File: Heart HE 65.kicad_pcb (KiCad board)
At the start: 2 copper layers, 303.8 x 94.2 mm, 290 parts, among them J2 Conn_01x04, SW1 SW_Push, U10 SLSS49E-3, U100 SLSS49E-3, U101 SLSS49E-3, U102 SLSS49E-3, U103 SLSS49E-3, U104 SLSS49E-3, U11 SLSS49E-3, U12 SLSS49E-3, U14 SLSS49E-3, U15 SLSS49E-3, U16 SLSS49E-3, U17 SLSS49E-3, U18 SLSS49E-3, U19 AP2112K-3.3, U2 74HC4051, U20 SLSS49E-3, U21 SLSS49E-3, U22 SLSS49E-3, U23 SLSS49E-3, U24 SLSS49E-3, U25 SLSS49E-3, U26 SLSS49E-3, U27 AT32F405KxU7-4, U28 SLSS49E-3, U29 SLSS49E-3, U3 SLSS49E-3, U30 SLSS49E-3, U31 SLSS49E-3, U32 74HC4051, U33 SLSS49E-3, U34 SLSS49E-3, U35 SLSS49E-3, U36 SLSS49E-3, U37 SLSS49E-3, U38 74HC4051, U4 SLSS49E-3, U40 SLSS49E-3, U41 SLSS49E-3, U42 SLSS49E-3, U43 SLSS49E-3, U44 SLSS49E-3, U45 74HC4051, U46 SLSS49E-3, U47 SLSS49E-3, U48 SLSS49E-3, U49 SLSS49E-3, U5 SLSS49E-3, U51 74HC4051, U52 SLSS49E-3, U53 SLSS49E-3, U54 SLSS49E-3, U55 SLSS49E-3, U56 74HC4051, U58 SLSS49E-3, U59 SLSS49E-3, U6 SLSS49E-3, U60 SLSS49E-3, U61 SLSS49E-3, U62 74HC4051, U63 AMS1117-3.3, U64 SLSS49E-3, U65 SLSS49E-3, U66 SLSS49E-3, U67 SLSS49E-3, U69 74HC4051, U7 SLSS49E-3, U70 SLSS49E-3, U71 SLSS49E-3, U72 SLSS49E-3, U73 SLSS49E-3, U74 74HC4051, U75 SLSS49E-3, U76 SLSS49E-3, U77 SLSS49E-3, U78 SLSS49E-3, U79 SLSS49E-3, U8 SLSS49E-3, U80 SLSS49E-3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

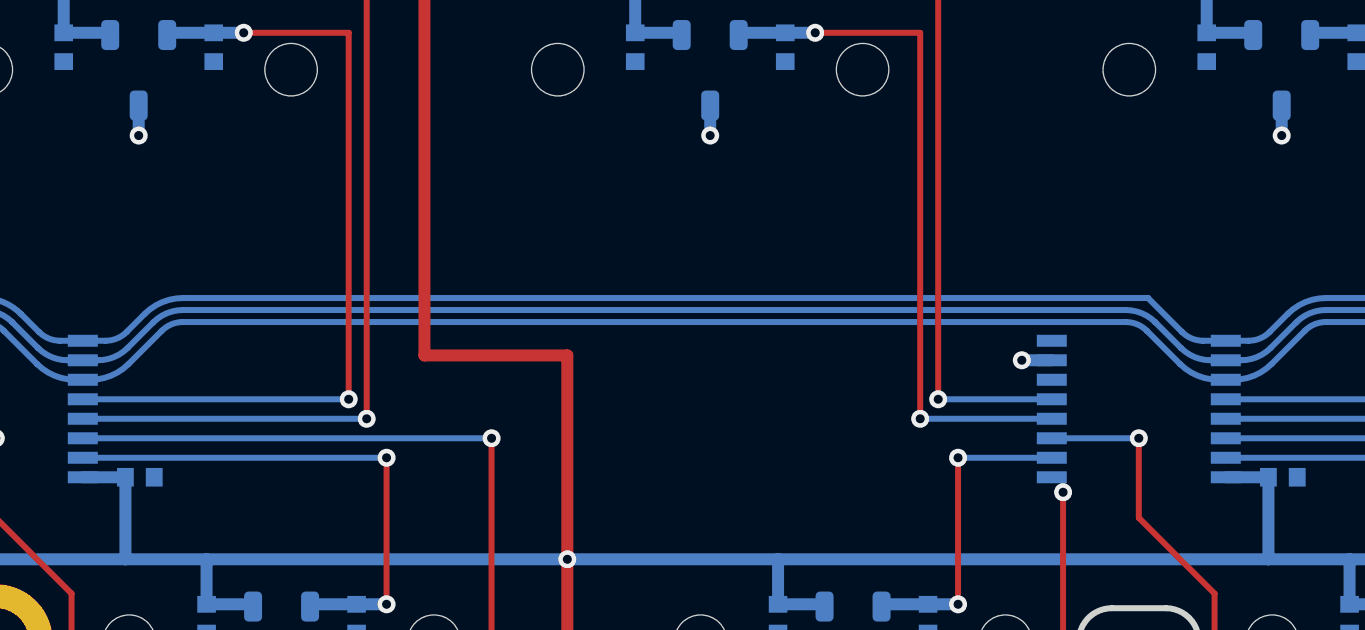
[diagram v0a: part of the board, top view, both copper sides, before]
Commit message: Update Heart HE 65.kicad_pcb
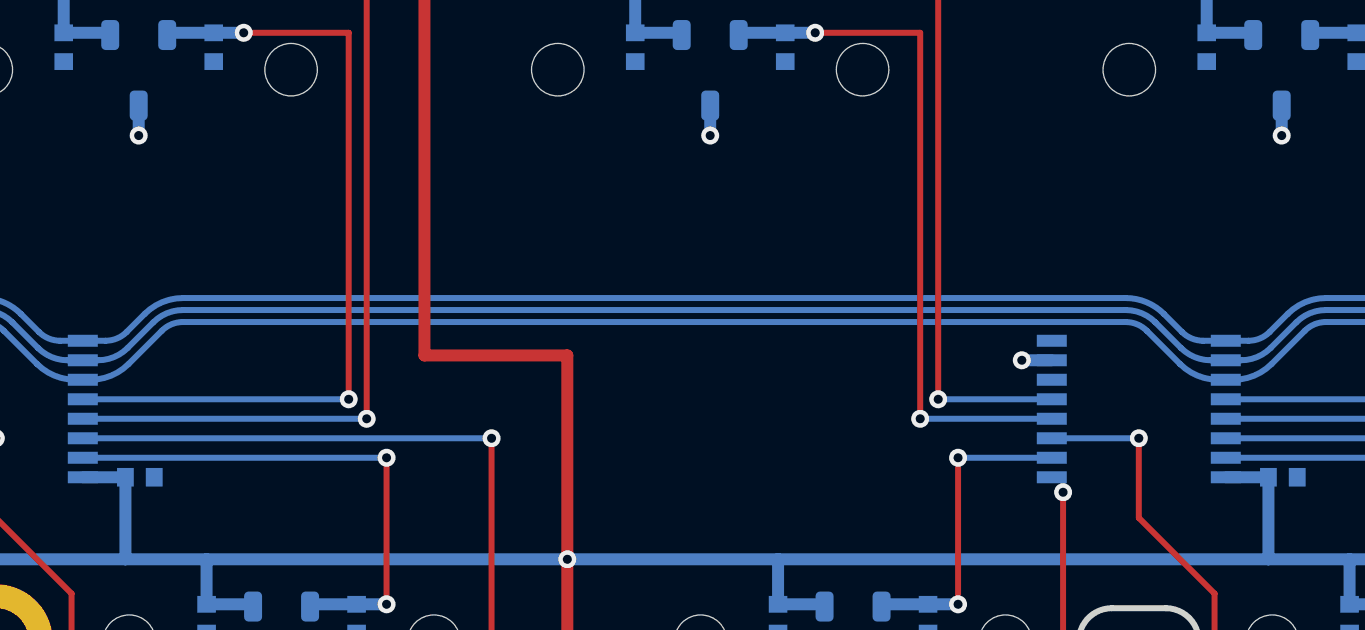
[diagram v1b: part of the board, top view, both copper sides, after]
